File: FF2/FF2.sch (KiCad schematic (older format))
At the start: 53 parts

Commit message: added extra row for the 5-way
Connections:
- net COL4: no longer MX17.1 (COL), MX18.1 (COL), MX19.1 (COL), MX20.1 (COL), MX21.1 (COL)
- new net COL5: MX17.1 (COL), MX18.1 (COL), MX19.1 (COL), MX20.1 (COL), MX21.1 (COL)
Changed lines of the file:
@@
 COL3
 Text GLabel 10900 950  1    50   Input ~ 0
-COL4
+COL5
 Wire Wire Line
 	7650 950  7650 1300
@@
 Wire Wire Line
 	9100 4600 10550 4600
+Text GLabel 10000 950  1    50   Input ~ 0
+COL4
 $EndSCHEMATC

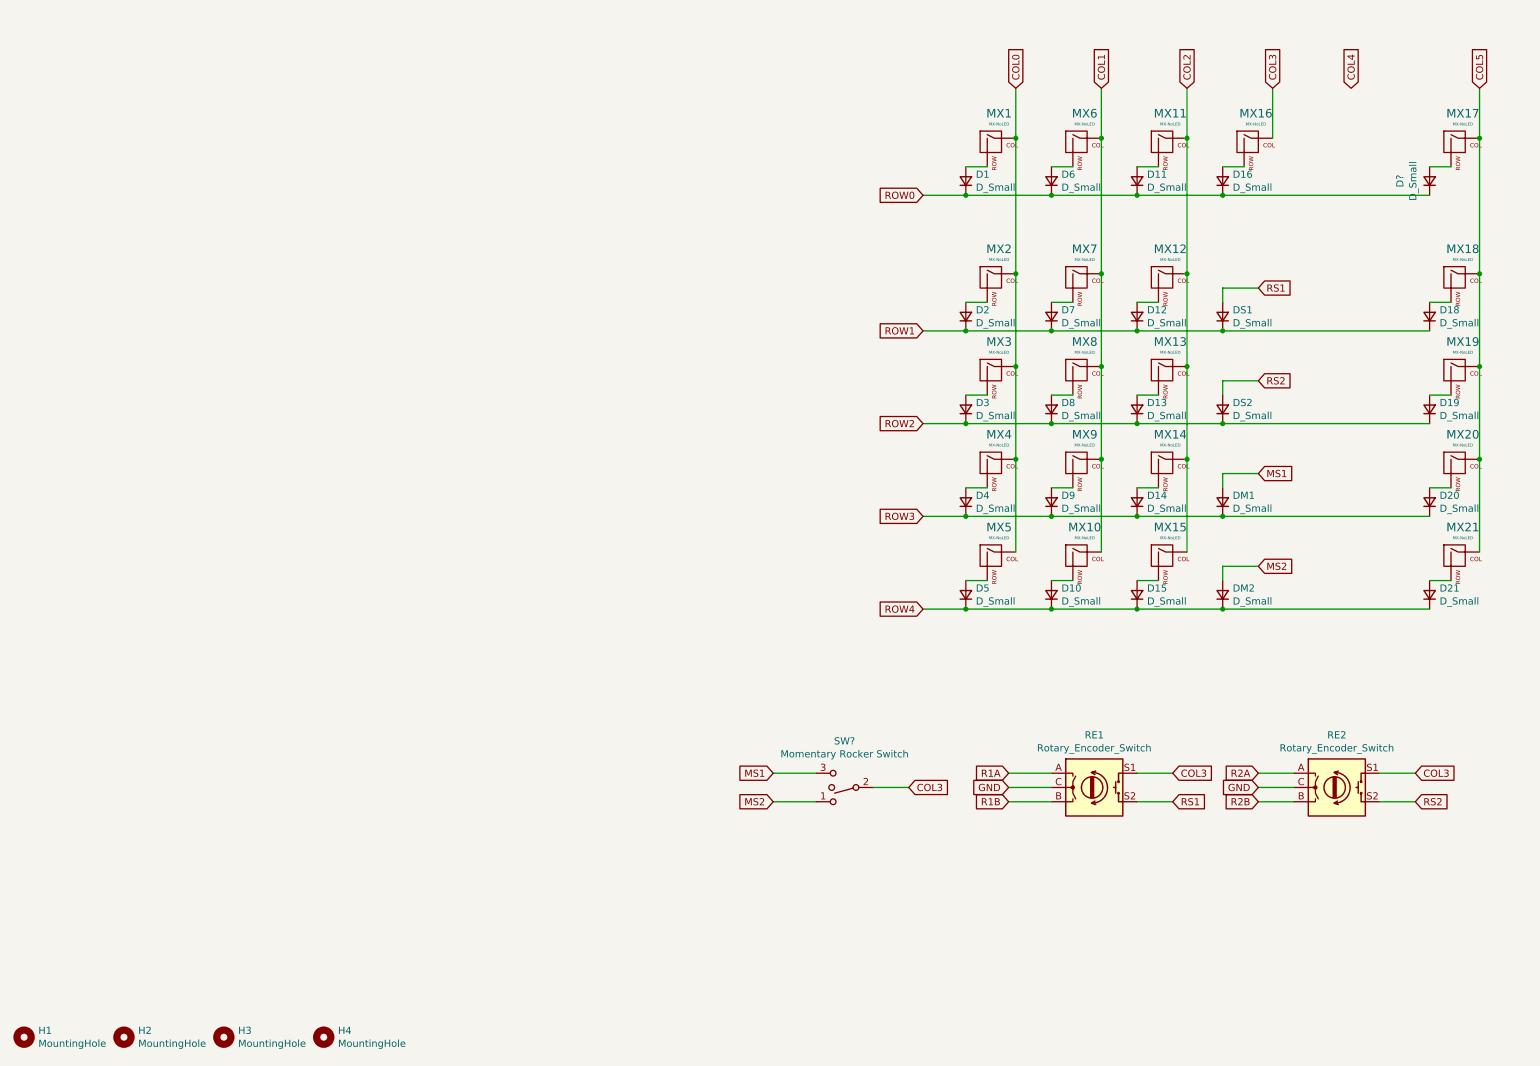
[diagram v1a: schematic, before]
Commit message: added rest of the components
using atmega328p with an USB-C and SMD components
Dobber is missing
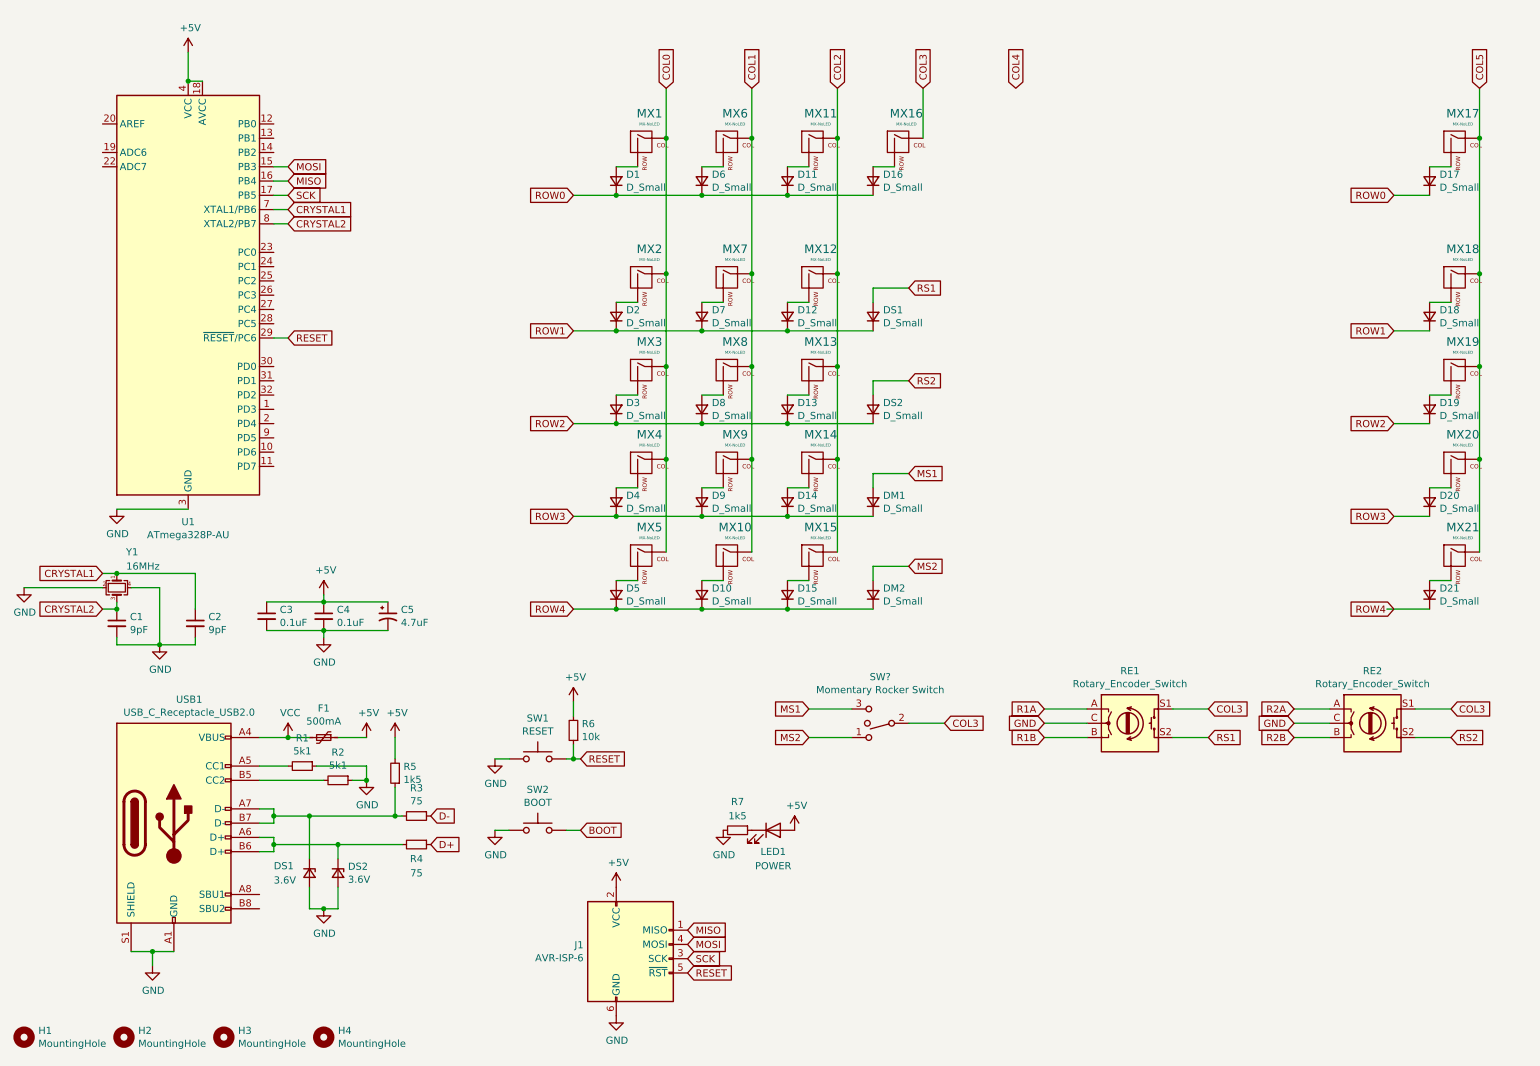
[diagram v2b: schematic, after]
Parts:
- removed D?: D_Small, symbol Device:D_Small
- added C1, C2: 9pF, Capacitor_SMD:C_0402_1005Metric, symbol Device:C_Small
- added C3, C4: 0.1uF, Capacitor_SMD:C_0603_1608Metric, symbol Device:C_Small
- added C5: 4.7uF, Capacitor_SMD:CP_Elec_4x5.3, symbol Device:CP1_Small
- added D17: D_Small, symbol Device:D_Small
- added DS1, DS2: 3.6V, Diode_SMD:D_SOD-123, symbol Device:D_Zener_Small
- added F1: 500mA, symbol Device:Polyfuse_Small
- added J1: AVR-ISP-6, symbol Connector:AVR-ISP-6
- added LED1: POWER, LED_SMD:LED_0805_2012Metric, symbol Device:LED
- added R1, R2: 5k1, Resistor_SMD:R_0603_1608Metric, symbol Device:R_Small
- added R3, R4: 75, Resistor_SMD:R_0603_1608Metric, symbol Device:R_Small
- added R5, R7: 1k5, Resistor_SMD:R_0603_1608Metric, symbol Device:R_Small
- added R6: 10k, Resistor_SMD:R_0603_1608Metric, symbol Device:R_Small
- added SW1: RESET, symbol Switch:SW_Push
- added SW2: BOOT, symbol Switch:SW_Push
- added U1: ATmega328P-AU, Package_QFP:TQFP-32_7x7mm_P0.8mm, symbol MCU_Microchip_ATmega:ATmega328P-AU
- added USB1: USB_C_Receptacle_USB2.0, symbol Connector:USB_C_Receptacle_USB2.0
- added Y1: 16MHz, Crystal:Crystal_SMD_2520-4Pin_2.5x2.0mm, symbol Device:Crystal_GND24_Small
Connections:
- net GND: now also C1.2, C2.2, C3.2, C4.2, C5.2, DS1.2 (A), DS2.2 (A), J1.6 (GND), R1.1, R2.1, R7.2, SW1.1, SW2.1, U1.21 (GND), U1.3 (GND), U1.5 (GND), USB1.A1 (GND), USB1.A12 (GND), USB1.B1 (GND), USB1.B12 (GND), USB1.S1 (SHIELD), Y1.2, Y1.4
- net ROW0: now also D17.1 (K)
- net at MX17.2 (ROW): now also D17.2 (A)
- new net: R1.2, USB1.A5 (CC1)
- new net: DS2.1 (K), R4.2, USB1.A6 (D+), USB1.B6 (D+)
- new net: DS1.1 (K), R3.2, R5.1, USB1.A7 (D-), USB1.B7 (D-)
- new net: R2.2, USB1.B5 (CC2)
- new net: LED1.1 (K), R7.1
- new net +5V: C3.1, C4.1, C5.1, F1.1, J1.2 (VCC), LED1.2 (A), R5.2, R6.2, U1.18 (AVCC), U1.4 (VCC), U1.6 (VCC)
- new net BOOT: SW2.2
- new net CRYSTAL1: C2.1, U1.7 (XTAL1/PB6), Y1.1
- new net CRYSTAL2: C1.1, U1.8 (XTAL2/PB7), Y1.3
- new net D+: R4.1
- new net D-: R3.1
- new net MISO: J1.1 (MISO), U1.16 (PB4)
- new net MOSI: J1.4 (MOSI), U1.15 (PB3)
- new net RESET: J1.5 (~RST), R6.1, SW1.2, U1.29 (~RESET~/PC6)
- new net SCK: J1.3 (SCK), U1.17 (PB5)
- new net VCC: F1.2, USB1.A4 (VBUS), USB1.A9 (VBUS), USB1.B4 (VBUS), USB1.B9 (VBUS)
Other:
- moved on the sheet: D1, D10, D11, D12, D13, D14, D15, D16, D2, D3, D4, D5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

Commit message: Added dobber symbol and footprint and wiring
added footprint for missing components, missing rocker switch
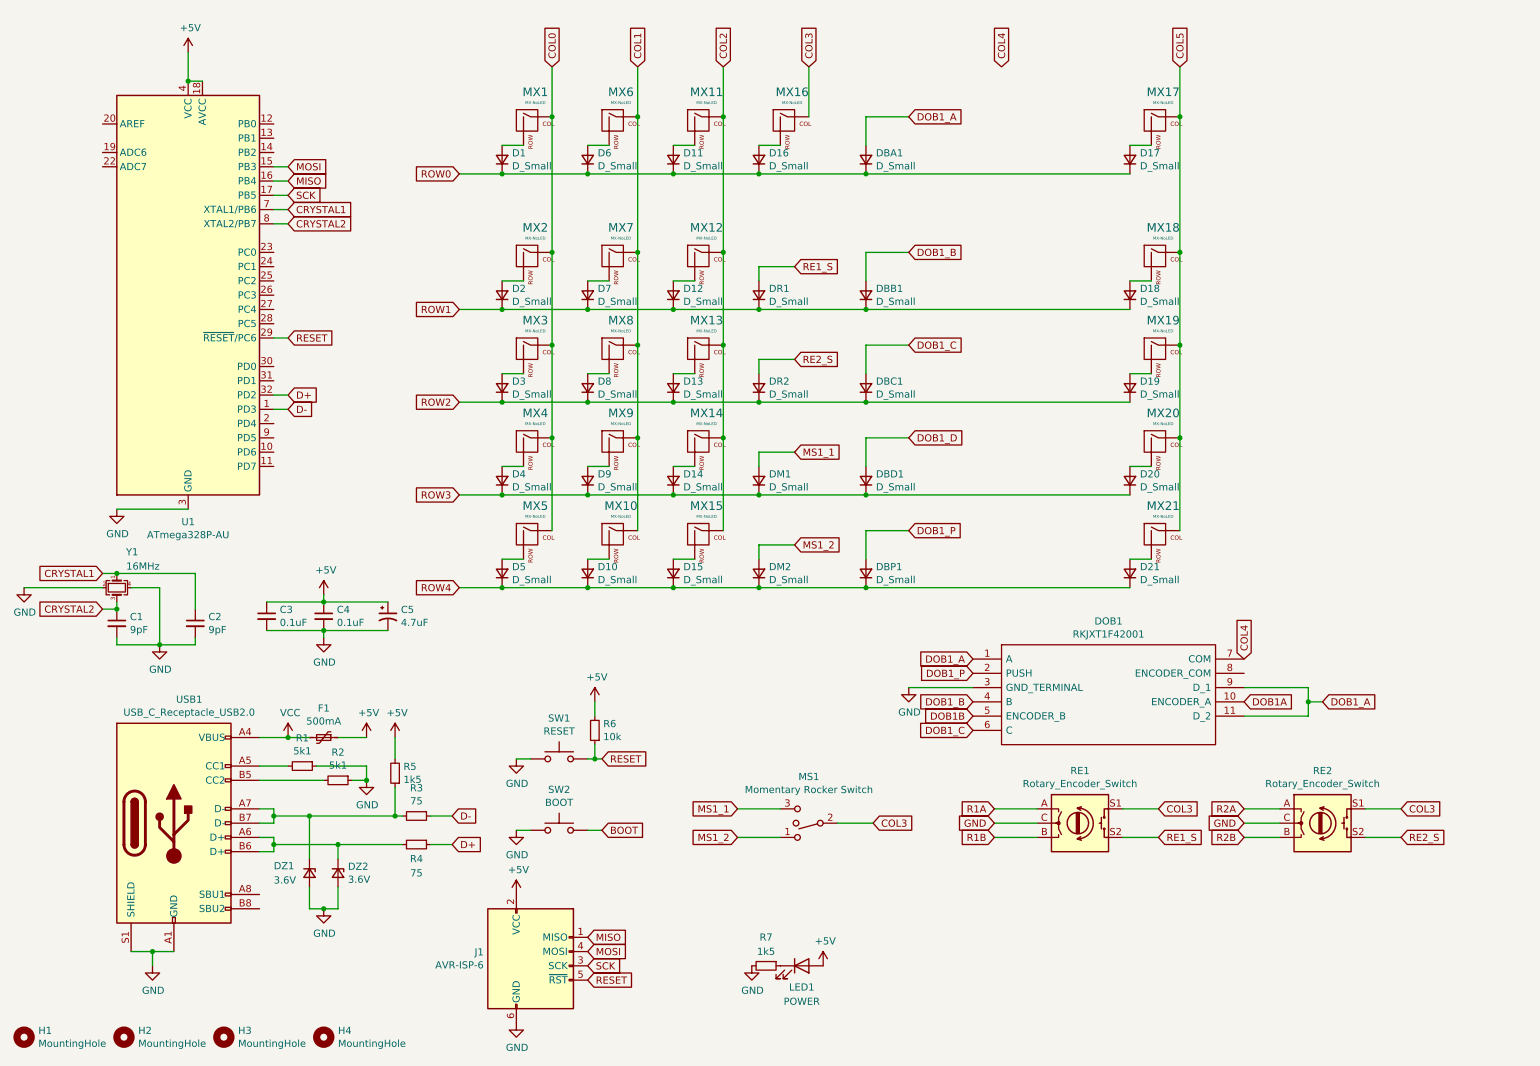
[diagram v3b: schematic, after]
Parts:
- added DBA1, DBB1, DBC1, DBD1, DBP1: D_Small, Diode_SMD:D_SOD-123, symbol Device:D_Small
- added DOB1: RKJXT1F42001, ALPS_RKJXT1F42001:RKJXT1F42001, symbol ALPS_RKJXT1F42001:RKJXT1F42001
- D1, D10, D11, D12, D13, D14, D15, D16, D17, D18, D19, D2, D20, D21, D3, D4, D5, D6, D7, D8, D9, DM1, DM2: footprint (none) -> Diode_SMD:D_SOD-123
- DR1: renamed from DS1; footprint (none) -> Diode_SMD:D_SOD-123
- DR2: renamed from DS2; footprint (none) -> Diode_SMD:D_SOD-123
- F1: footprint (none) -> Capacitor_THT:C_Disc_D5.0mm_W2.5mm_P5.00mm
- H1, H2, H3, H4: footprint (none) -> MountingHole:MountingHole_3.2mm_M3_Pad
- J1: footprint (none) -> random-keyboard-parts:Reset_Pretty-Mask
- MX1, MX10, MX11, MX12, MX13, MX14, MX15, MX16, MX17, MX18, MX19, MX2, MX20, MX21, MX3, MX4, MX5, MX6, MX7, MX8, MX9: footprint (none) -> MX_Alps_Hybrid:MX-1U-NoLED
- RE1, RE2: footprint (none) -> Rotary_Encoder:RotaryEncoder_Alps_EC11E-Switch_Vertical_H20mm
- gave numbers to parts that had none: 1
- renumbered DS1 to DZ1, DS2 to DZ2
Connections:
- net COL4: now also DOB1.7 (COM)
- net D+: now also U1.32 (PD2)
- net D-: now also U1.1 (PD3)
- net GND: now also DOB1.3 (GND_TERMINAL)
- net ROW0: now also DBA1.1 (K)
- net ROW1: now also DBB1.1 (K)
- net ROW2: now also DBC1.1 (K)
- net ROW3: now also DBD1.1 (K)
- net ROW4: now also DBP1.1 (K)
- net MS1 renamed MS1_1
- net MS2 renamed MS1_2
- net RS1 renamed RE1_S
- net RS2 renamed RE2_S
- new net DOB1A: DOB1.10 (ENCODER_A)
- new net DOB1B: DOB1.5 (ENCODER_B)
- new net DOB1_A: DBA1.2 (A), DOB1.1 (A), DOB1.11 (D_2), DOB1.9 (D_1)
- new net DOB1_B: DBB1.2 (A), DOB1.4 (B)
- new net DOB1_C: DBC1.2 (A), DOB1.6 (C)
- new net DOB1_D: DBD1.2 (A)
- new net DOB1_P: DBP1.2 (A), DOB1.2 (PUSH)
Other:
- moved on the sheet: D1, D10, D11, D12, D13, D14, D15, D16, D17, D18, D19, D2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

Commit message: added more footprint associations
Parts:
- SW1, SW2: footprint (none) -> Connector_PinHeader_1.00mm:PinHeader_1x02_P1.00mm_Vertical
- USB1: footprint (none) -> Connector_USB:USB_C_Receptacle_XKB_U262-16XN-4BVC11
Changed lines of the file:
@@
 F 0 "USB1" H 1857 6967 50  0000 C CNN
 F 1 "USB_C_Receptacle_USB2.0" H 1857 6876 50  0000 C CNN
-F 2 "" H 1900 6100 50  0001 C CNN
+F 2 "Connector_USB:USB_C_Receptacle_XKB_U262-16XN-4BVC11" H 1900 6100 50  0001 C CNN
 F 3 "https://www.usb.org/sites/default/files/documents/usb_type-c.zip" H 1900 6100 50  0001 C CNN
 	1    1750 6100
@@
 F 0 "SW1" H 4450 5935 50  0000 C CNN
 F 1 "RESET" H 4450 5844 50  0000 C CNN
-F 2 "" H 4450 5850 50  0001 C CNN
+F 2 "Connector_PinHeader_1.00mm:PinHeader_1x02_P1.00mm_Vertical" H 4450 5850 50  0001 C CNN
 F 3 "~" H 4450 5850 50  0001 C CNN
 	1    4450 5650
@@
 F 0 "SW2" H 4450 6435 50  0000 C CNN
 F 1 "BOOT" H 4450 6344 50  0000 C CNN
-F 2 "" H 4450 6350 50  0001 C CNN
+F 2 "Connector_PinHeader_1.00mm:PinHeader_1x02_P1.00mm_Vertical" H 4450 6350 50  0001 C CNN
 F 3 "~" H 4450 6350 50  0001 C CNN
 	1    4450 6150

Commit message: updated switches footprints lib, start of placement on board
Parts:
- H1, H2, H3, H4: footprint MountingHole:MountingHole_3.2mm_M3_Pad -> MountingHole:MountingHole_3.2mm_M3_ISO7380_Pad
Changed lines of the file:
@@
 F 0 "H4" H 2900 7646 50  0000 L CNN
 F 1 "MountingHole" H 2900 7555 50  0000 L CNN
-F 2 "MountingHole:MountingHole_3.2mm_M3_Pad" H 2800 7600 50  0001 C CNN
+F 2 "MountingHole:MountingHole_3.2mm_M3_ISO7380_Pad" H 2800 7600 50  0001 C CNN
 F 3 "~" H 2800 7600 50  0001 C CNN
 	1    2800 7600
@@
 F 0 "H1" H 800 7646 50  0000 L CNN
 F 1 "MountingHole" H 800 7555 50  0000 L CNN
-F 2 "MountingHole:MountingHole_3.2mm_M3_Pad" H 700 7600 50  0001 C CNN
+F 2 "MountingHole:MountingHole_3.2mm_M3_ISO7380_Pad" H 700 7600 50  0001 C CNN
 F 3 "~" H 700 7600 50  0001 C CNN
 	1    700  7600
@@
 F 0 "H2" H 1500 7646 50  0000 L CNN
 F 1 "MountingHole" H 1500 7555 50  0000 L CNN
-F 2 "MountingHole:MountingHole_3.2mm_M3_Pad" H 1400 7600 50  0001 C CNN
+F 2 "MountingHole:MountingHole_3.2mm_M3_ISO7380_Pad" H 1400 7600 50  0001 C CNN
 F 3 "~" H 1400 7600 50  0001 C CNN
 	1    1400 7600
@@
 F 0 "H3" H 2200 7646 50  0000 L CNN
 F 1 "MountingHole" H 2200 7555 50  0000 L CNN
-F 2 "MountingHole:MountingHole_3.2mm_M3_Pad" H 2100 7600 50  0001 C CNN
+F 2 "MountingHole:MountingHole_3.2mm_M3_ISO7380_Pad" H 2100 7600 50  0001 C CNN
 F 3 "~" H 2100 7600 50  0001 C CNN
 	1    2100 7600

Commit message: trace routing
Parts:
- removed DBA1, DBB1, DBC1, DBD1, DBP1: D_Small, Diode_SMD:D_SOD-123, symbol Device:D_Small
- added DB1: D_Small, Diode_SMD:D_SOD-123, symbol Device:D_Small
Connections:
- net COL5 is gone; now on net COL4: MX17.1 (COL), MX18.1 (COL), MX19.1 (COL), MX20.1 (COL), MX21.1 (COL)
- net DOB1_B is gone; now on net COL1: DOB1.4 (B)
- net DOB1_C is gone; now on net COL2: DOB1.6 (C)
- net DOB1_P is gone; now on net COL4: DOB1.2 (PUSH)
- net ROW0 is gone; now on net BOOT: D1.1 (K), D11.1 (K), D16.1 (K), D17.1 (K), D6.1 (K)
- net BOOT: now also U1.9 (PD5)
- net COL0: now also DOB1.1 (A)
- net COL3: now also DOB1.11 (D_2), DOB1.9 (D_1)
- net COL4: no longer DOB1.7 (COM)
- net ROW1: now also U1.10 (PD6)
- net ROW2: now also U1.11 (PD7)
- net ROW3: now also U1.12 (PB0)
- net ROW4: now also U1.13 (PB1)
- net ROW5: now reaches U1.14 (PB2)
- net ROW5: now also DB1.1 (K)
- removed net DOB1_A: DOB1.1 (A), DOB1.11 (D_2), DOB1.9 (D_1)
- new net DOB1_COM: DB1.2 (A), DOB1.7 (COM)
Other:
- moved on the sheet: C1, C2, C3, C4, C5, D1, D10, D11, D12, D13, D14, D15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

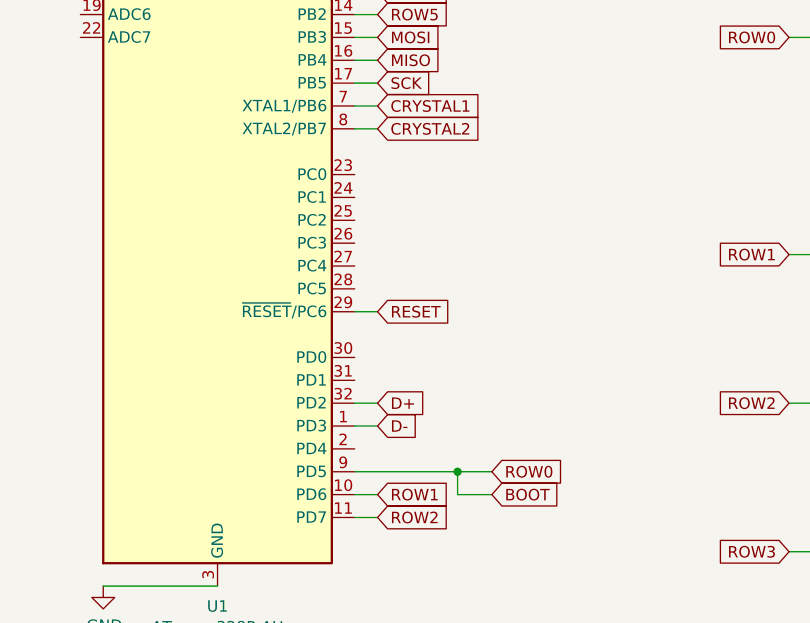
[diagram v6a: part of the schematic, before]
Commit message: more routing, only dobber and 2-way missing
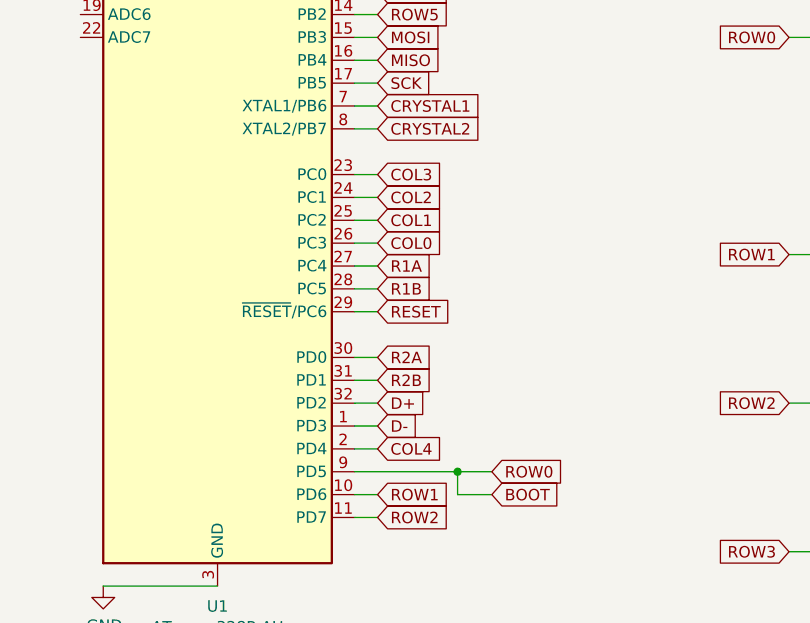
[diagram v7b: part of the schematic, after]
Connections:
- net COL0: now also U1.26 (PC3)
- net COL1: now also U1.25 (PC2)
- net COL2: now also U1.24 (PC1)
- net COL3: now also U1.23 (PC0)
- net COL4: now also U1.2 (PD4)
- net R1A: now also U1.27 (PC4)
- net R1B: now also U1.28 (PC5)
- net R2A: now also U1.30 (PD0)
- net R2B: now also U1.31 (PD1)
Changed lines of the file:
@@
 	2900 3400 2450 3400
 Connection ~ 2900 3400
+Text GLabel 2550 3300 2    50   Input ~ 0
+COL4
+Wire Wire Line
+	2550 3300 2450 3300
+Text GLabel 2550 2100 2    50   Input ~ 0
+COL3
+Text GLabel 2550 2200 2    50   Input ~ 0
+COL2
+Text GLabel 2550 2300 2    50   Input ~ 0
+COL1
+Text GLabel 2550 2400 2    50   Input ~ 0
+COL0
+Wire Wire Line
+	2550 2100 2450 2100
+Wire Wire Line
+	2450 2200 2550 2200
+Wire Wire Line
+	2550 2300 2450 2300
+Wire Wire Line
+	2450 2400 2550 2400
+Text GLabel 2550 2500 2    50   Input ~ 0
+R1A
+Text GLabel 2550 2600 2    50   Input ~ 0
+R1B
+Text GLabel 2550 2900 2    50   Input ~ 0
+R2A
+Text GLabel 2550 3000 2    50   Input ~ 0
+R2B
+Wire Wire Line
+	2550 3000 2450 3000
+Wire Wire Line
+	2450 2900 2550 2900
+Wire Wire Line
+	2550 2600 2450 2600
+Wire Wire Line
+	2450 2500 2550 2500
 $EndSCHEMATC

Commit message: updated with all SMD on the front and part numbers for production
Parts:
- C1, C2: LCSC (none) -> C111805
- C3, C4: LCSC (none) -> C14663
- C5: LCSC (none) -> C134741
- D1, D10, D11, D12, D13, D14, D15, D16, D17, D18, D19, D2, D20, D21, D3, D4, D5, D6, D7, D8, D9, DB1, DM1, DM2, DR1, DR2: footprint Diode_SMD:D_SOD-123 -> Diode_SMD:D_SOD-123F; LCSC (none) -> C426570
- DOB1: LCSC (none) -> C160841
- DZ1, DZ2: LCSC (none) -> C82565
- F1: LCSC (none) -> C208476
- LED1: LCSC (none) -> C205442
- MX1, MX10, MX11, MX12, MX13, MX14, MX15, MX16, MX17, MX18, MX19, MX2, MX20, MX21, MX3, MX4, MX5, MX6, MX7, MX8, MX9: LCSC (none) -> C400228
- R1, R2: LCSC (none) -> C23186
- R3, R4: LCSC (none) -> C4275
- R5, R7: LCSC (none) -> C22843
- R6: LCSC (none) -> C25804
- RE1, RE2: LCSC (none) -> C255515
- U1: LCSC (none) -> C14877
- USB1: LCSC (none) -> C393939
- Y1: LCSC (none) -> C280090
